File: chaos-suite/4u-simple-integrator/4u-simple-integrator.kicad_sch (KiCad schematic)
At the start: 31 parts

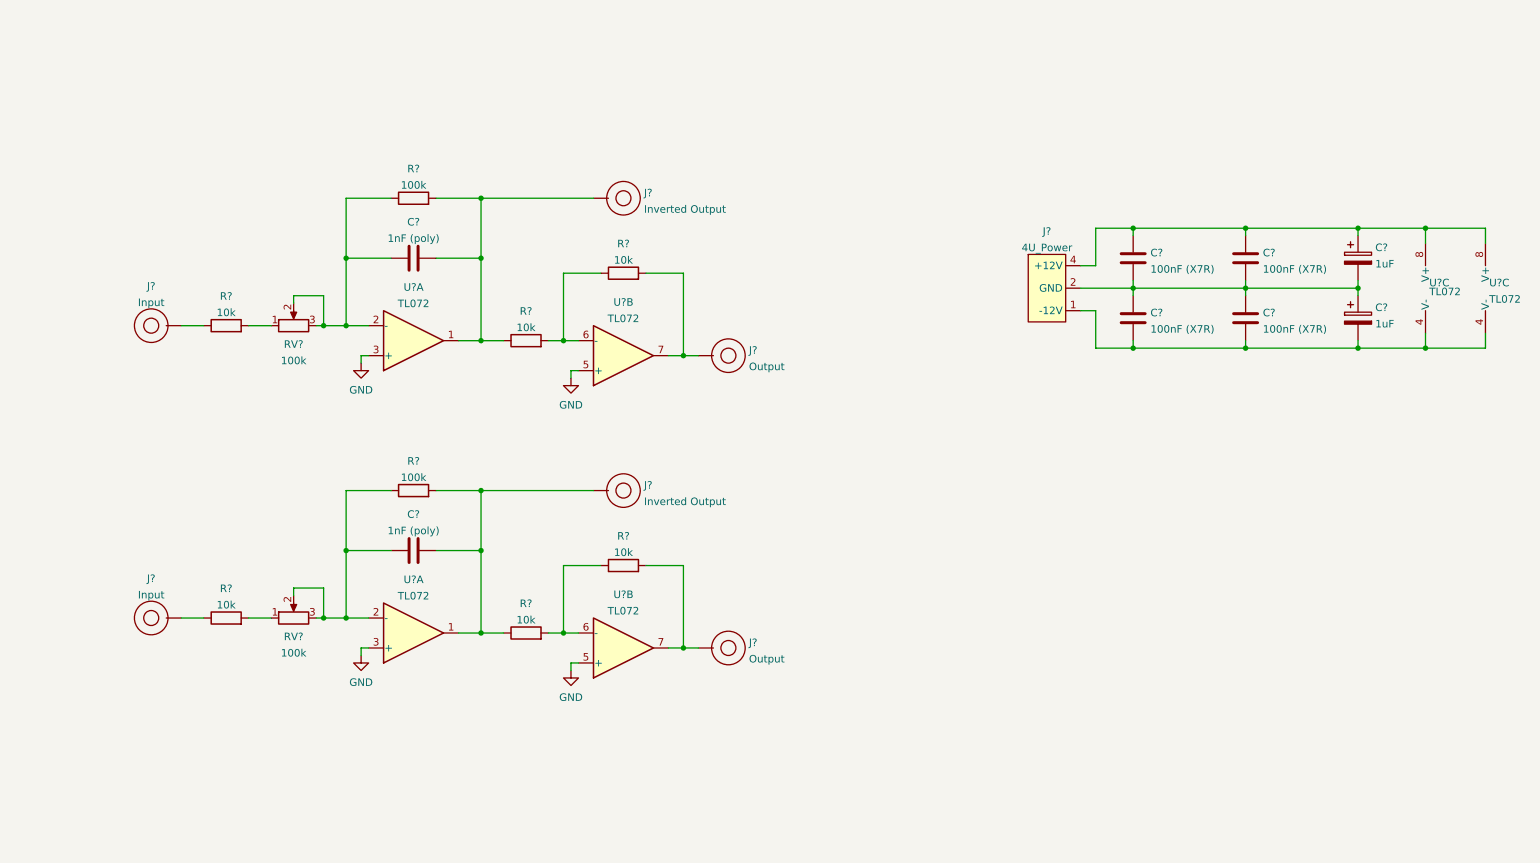
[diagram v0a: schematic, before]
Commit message: Adding first chaos suite modules
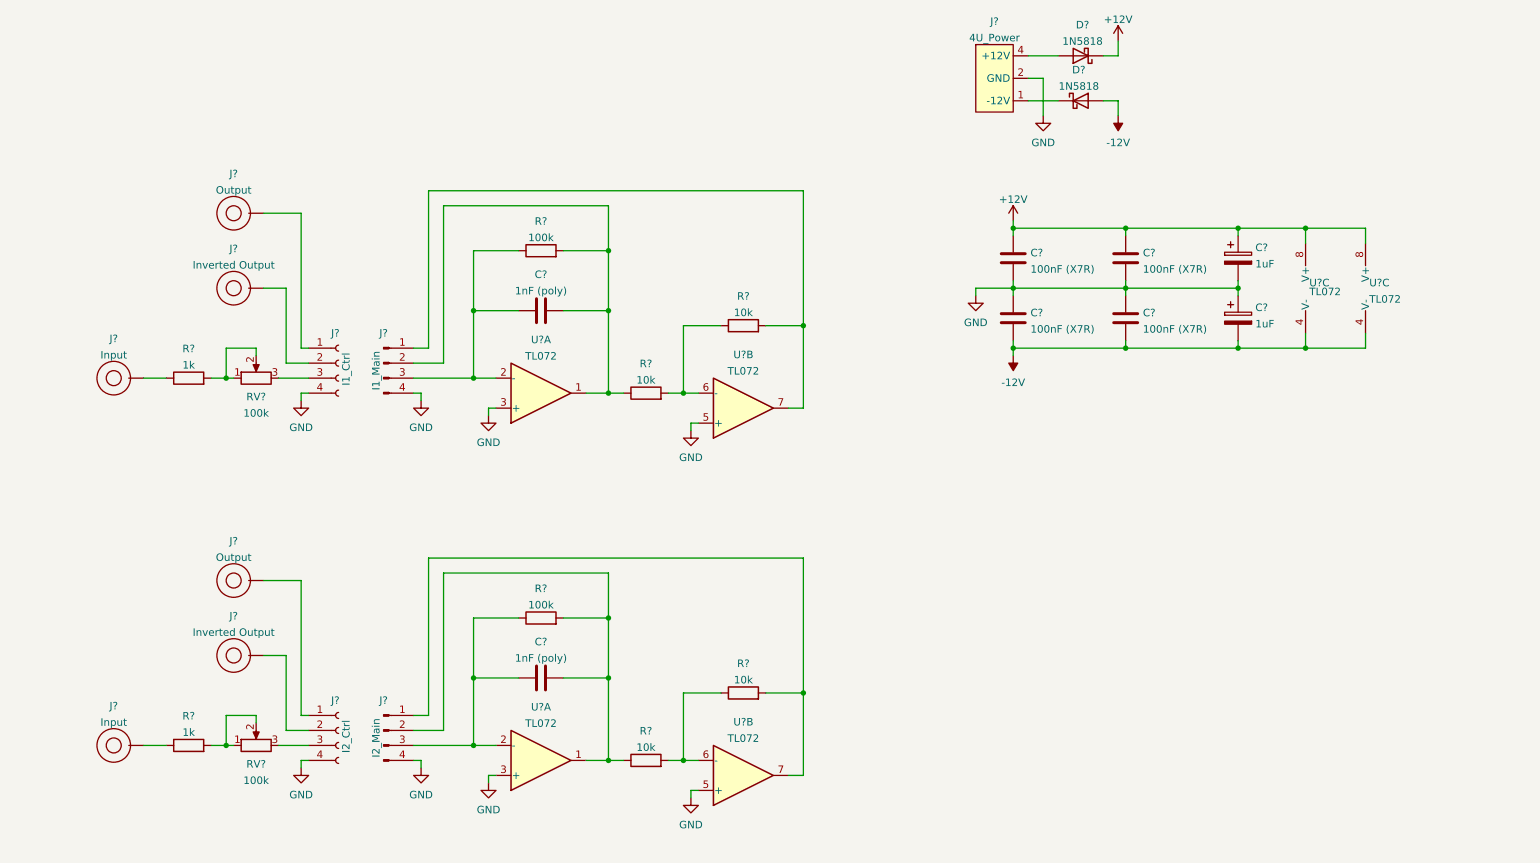
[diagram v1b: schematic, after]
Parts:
- removed C?: 1nF (poly), symbol Device:C
- removed J? (x3): BananaJack_PanelMount, symbol BananaJacks:BananaJack_PanelMount
- removed R?: 100k, symbol Device:R
- removed R? (x3): 10k, symbol Device:R
- removed RV?: 100k, symbol Device:R_Potentiometer
- removed U? (x2): TL072, symbol Amplifier_Operational:TL072
- added C?: 1nF (poly), symbol Device:C
- added D? (x2): 1N5818, Diode_THT:D_DO-41_SOD81_P10.16mm_Horizontal, symbol Diode:1N5818
- added J?: I1_Ctrl, symbol Connector:Conn_01x04_Female
- added J? (x3): BananaJack_PanelMount, symbol BananaJacks:BananaJack_PanelMount
- added J?: I2_Main, symbol Connector:Conn_01x04_Male
- added J?: I2_Ctrl, symbol Connector:Conn_01x04_Female
- added J?: I1_Main, symbol Connector:Conn_01x04_Male
- added R?: 100k, symbol Device:R
- added R? (x2): 10k, symbol Device:R
- added R?: 1k, symbol Device:R
- added RV?: 100k, symbol Device:R_Potentiometer
- added U? (x2): TL072, symbol Amplifier_Operational:TL072
- R?: value 10k -> 1k
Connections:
- net GND: now also C?.1, C?.1, C?.1, C?.2, C?.2, C?.2, J?.2 (GND), J?.3 (GND), J?.4 (Pin_4), J?.4 (Pin_4), J?.4 (Pin_4), J?.4 (Pin_4), U?.3 (+), U?.5 (+)
- net -12V: now reaches C?.2, C?.2, C?.2, U?.4 (V-), U?.4 (V-)
- net -12V: now also D?.2 (A); no longer J?.1 (-12V)
- net +12V: now reaches C?.1, C?.1, C?.1, U?.8 (V+), U?.8 (V+)
- net +12V: now also D?.1 (K); no longer J?.4 (+12V)
- net at C?.2, R?.1, R?.2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: now also J?.2 (Pin_2); no longer J?.1
- net at R?.2, RV?.1: now also RV?.2
- net at C?.1, R?.1, U?.2 (-): now also J?.3 (Pin_3); no longer RV?.2, RV?.3
- net at R?.2, U?.7: now also J?.1 (Pin_1); no longer J?.1
- new net: D?.1 (K), J?.1 (-12V)
- new net: D?.2 (A), J?.4 (+12V)
- new net: J?.1, J?.1 (Pin_1) (x2)
- new net: J?.1, J?.2 (Pin_2) (x2)
- new net: J?.3 (Pin_3), RV?.3 (x2)
- new net: C?.1, J?.3 (Pin_3), R?.1, U?.2 (-)
- new net: C?.2, J?.2 (Pin_2), R?.1, R?.2, U?.1
- new net: R?.1, R?.2, U?.6 (-)
- new net: J?.1 (Pin_1), R?.2, U?.7
- new net: J?.1, R?.1
- new net: R?.2, RV?.1, RV?.2
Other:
- moved on the sheet: C?, J?, R?, RV?, U?A, U?B, U?C

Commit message: Final tweaks to simple integrator
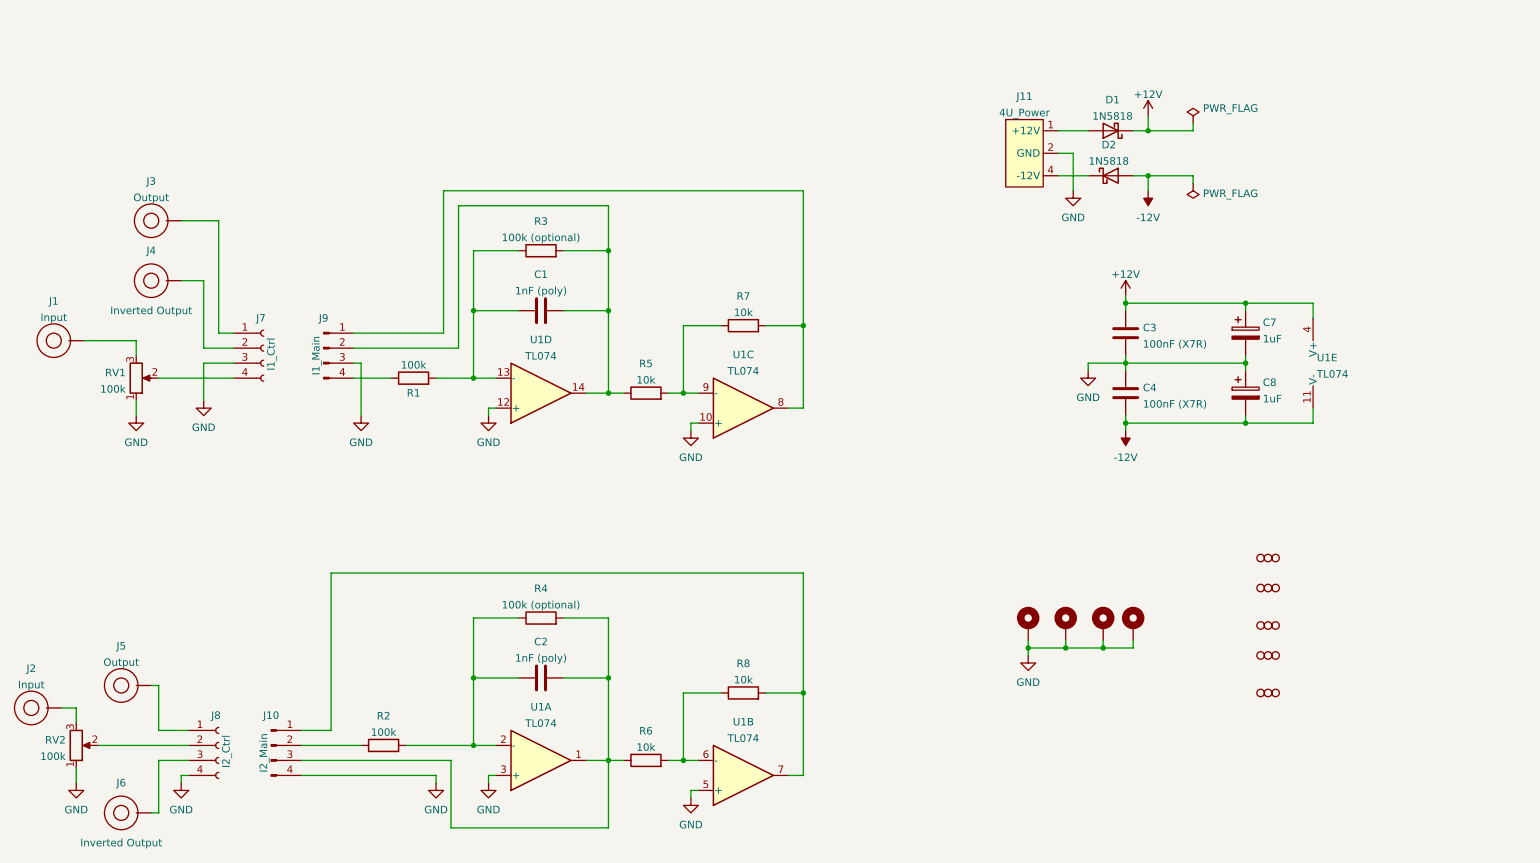
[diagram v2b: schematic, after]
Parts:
- removed C? (x2): 100nF (X7R), symbol Device:C
- removed U? (x6): TL072, symbol Amplifier_Operational:TL072
- added H1, H2, H3, H4: MountingHole_Pad, MountingHole:MountingHole_3.2mm_M3_Pad, symbol Mechanical:MountingHole_Pad
- added H5, H6, H7, H8, H9: MouseBite, Panelization:mouse-bite-2.54mm-slot, symbol Panelization:MouseBite
- added U1: TL074, Rumblesan_Footprints:DIP-14_W7.62mm_Socket, symbol Amplifier_Operational:TL074
- C1, C2, C3, C4: renamed from C?; footprint (none) -> Rumblesan_Footprints:C_Rect_L7.0mm_W3.5mm_P5.00mm
- C7, C8: renamed from C?; footprint (none) -> Capacitor_THT:CP_Radial_D5.0mm_P2.00mm
- D1, D2: renamed from D?; footprint Diode_THT:D_DO-41_SOD81_P10.16mm_Horizontal -> Rumblesan_Footprints:D_DO-41_SOD81_P10.16mm_Horizontal
- J1, J2, J3, J4, J5, J6: renamed from J?; footprint (none) -> Rumblesan_Footprints:BananaJack_THT_JohnsonCinch_108-09
- J10, J9: renamed from J?; footprint (none) -> Connector_PinHeader_2.54mm:PinHeader_1x04_P2.54mm_Vertical
- J11: renamed from J?; footprint (none) -> Rumblesan_Footprints:4u_Power_Molex_KK-254_P2.54mm
- J7, J8: renamed from J?; footprint (none) -> Connector_PinSocket_2.54mm:PinSocket_1x04_P2.54mm_Vertical
- R1, R2: renamed from R?; value 1k -> 100k; footprint (none) -> Rumblesan_Footprints:Resistor_THT_L6.3mm_D2.5mm_P10.16mm_Horizontal
- R3, R4: renamed from R?; value 100k -> 100k (optional); footprint (none) -> Rumblesan_Footprints:Resistor_THT_L6.3mm_D2.5mm_P10.16mm_Horizontal
- R5, R6, R7, R8: renamed from R?; footprint (none) -> Rumblesan_Footprints:Resistor_THT_L6.3mm_D2.5mm_P10.16mm_Horizontal
- RV1, RV2: renamed from RV?; footprint (none) -> Rumblesan_Footprints:Potentiometer_Alpha_RD901F-40-00D_Single_Vertical_CircularHoles
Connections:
- net +12V: now also U1.4 (V+)
- net -12V: now also U1.11 (V-)
- net GND: now also J7.3 (Pin_3), J9.3 (Pin_3), RV1.1, RV2.1, H1.1, H2.1, H3.1, H4.1, U1.10 (+), U1.12 (+), U1.3 (+), U1.5 (+); no longer J7.4 (Pin_4), J9.4 (Pin_4)
- net at J11.1 (+12V): now also D1.2 (A); no longer D2.1 (K)
- net at J11.4 (-12V): now also D2.1 (K); no longer D1.2 (A)
- net at RV1.3: now also J1.1; no longer J7.3 (Pin_3)
- net at J6.1: now also J8.3 (Pin_3); no longer J8.2 (Pin_2)
- net at C2.2, R4.2, R6.1: now also J10.3 (Pin_3), U1.1; no longer J10.2 (Pin_2)
- net at R6.2, R8.1: now also U1.6 (-)
- net at J2.1: now also RV2.3; no longer R2.1
- net at C1.1, R3.1: now also R1.2, U1.13 (-); no longer J9.3 (Pin_3)
- net at C1.2, J9.2 (Pin_2), R3.2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: now also U1.14
- net at J10.1 (Pin_1), R8.2: now also U1.7
- net at C2.1, R4.1: now also R2.2, U1.2 (-); no longer J10.3 (Pin_3)
- net at R5.2, R7.1: now also U1.9 (-)
- net at J9.1 (Pin_1), R7.2: now also U1.8
- net at R1.1: now also J9.4 (Pin_4); no longer J1.1
- new net: J7.4 (Pin_4), RV1.2
- new net: J10.2 (Pin_2), R2.1
- new net: J8.2 (Pin_2), RV2.2
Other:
- title: (none) -> Simple Integrator
- moved on the sheet: C3, C4, C7, C8, D1, D2, J1, J10, J11, J2, J3, J4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

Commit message: Updating simple integrator to rev2
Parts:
- removed H5, H6, H7, H8, H9: MouseBite, Panelization:mouse-bite-2.54mm-slot, symbol Panelization:MouseBite
- added R10, R3, R4, R9: 330r, rumblesan-standard-parts:R_Axial_DIN0207_L6.3mm_D2.5mm_P10.16mm_Horizontal, symbol rumblesan-standard-parts:R
- C1, C2: value 1nF (poly) -> 1nF; footprint Rumblesan_Footprints:C_Rect_L7.0mm_W3.5mm_P5.00mm -> rumblesan-standard-parts:C_Rect_L7.0mm_W3.5mm_P5.00mm; symbol Device:C -> rumblesan-standard-parts:C; Spec (none) -> film; Tolerance (none) -> 5%
- C3, C4: value 100nF (X7R) -> 100nF; footprint Rumblesan_Footprints:C_Rect_L7.0mm_W3.5mm_P5.00mm -> rumblesan-standard-parts:C_Rect_L7.0mm_W3.5mm_P5.00mm; symbol Device:C -> rumblesan-standard-parts:C; Spec (none) -> ceramic X7R; Tolerance (none) -> 5%
- C5: renamed from C7; value 1uF -> 10uF; footprint Capacitor_THT:CP_Radial_D5.0mm_P2.00mm -> rumblesan-standard-parts:CP_Radial_D5.0mm_P2.00mm; symbol Device:C_Polarized -> rumblesan-standard-parts:C_Polarized; Spec (none) -> electrolytic; Tolerance (none) -> 20%; Voltage (none) -> 50v
- C6: renamed from C8; value 1uF -> 10uF; footprint Capacitor_THT:CP_Radial_D5.0mm_P2.00mm -> rumblesan-standard-parts:CP_Radial_D5.0mm_P2.00mm; symbol Device:C_Polarized -> rumblesan-standard-parts:C_Polarized; Spec (none) -> electrolytic; Tolerance (none) -> 20%; Voltage (none) -> 50v
- D1, D2: footprint Rumblesan_Footprints:D_DO-41_SOD81_P10.16mm_Horizontal -> rumblesan-standard-parts:D_DO-41_SOD81_P10.16mm_Horizontal
- H1, H2, H3, H4: now left out of the parts list
- J1: renamed from J2; footprint Rumblesan_Footprints:BananaJack_THT_JohnsonCinch_108-09 -> rumblesan-standard-parts:BananaJack_THT_JohnsonCinch_108-09; symbol BananaJacks:BananaJack_PanelMount -> BananaJacks:Banana Socket PanelMount
- J11: footprint Rumblesan_Footprints:4u_Power_Molex_KK-254_P2.54mm -> 4u-power:4u_Power_Molex_KK-254_P2.54mm
- J2: renamed from J1; footprint Rumblesan_Footprints:BananaJack_THT_JohnsonCinch_108-09 -> rumblesan-standard-parts:BananaJack_THT_JohnsonCinch_108-09; symbol BananaJacks:BananaJack_PanelMount -> BananaJacks:Banana Socket PanelMount
- J3: renamed from J5; footprint Rumblesan_Footprints:BananaJack_THT_JohnsonCinch_108-09 -> rumblesan-standard-parts:BananaJack_THT_JohnsonCinch_108-09; symbol BananaJacks:BananaJack_PanelMount -> BananaJacks:Banana Socket PanelMount
- J4: renamed from J6; footprint Rumblesan_Footprints:BananaJack_THT_JohnsonCinch_108-09 -> rumblesan-standard-parts:BananaJack_THT_JohnsonCinch_108-09; symbol BananaJacks:BananaJack_PanelMount -> BananaJacks:Banana Socket PanelMount
- J5: renamed from J3; footprint Rumblesan_Footprints:BananaJack_THT_JohnsonCinch_108-09 -> rumblesan-standard-parts:BananaJack_THT_JohnsonCinch_108-09; symbol BananaJacks:BananaJack_PanelMount -> BananaJacks:Banana Socket PanelMount
- J6: renamed from J4; footprint Rumblesan_Footprints:BananaJack_THT_JohnsonCinch_108-09 -> rumblesan-standard-parts:BananaJack_THT_JohnsonCinch_108-09; symbol BananaJacks:BananaJack_PanelMount -> BananaJacks:Banana Socket PanelMount
- R1: renamed from R2; footprint Rumblesan_Footprints:Resistor_THT_L6.3mm_D2.5mm_P10.16mm_Horizontal -> rumblesan-standard-parts:R_Axial_DIN0207_L6.3mm_D2.5mm_P10.16mm_Horizontal; symbol Device:R -> rumblesan-standard-parts:R; Power (none) -> 0.5W; Spec (none) -> metal film; Tolerance (none) -> 1%
- R11: renamed from R7; footprint Rumblesan_Footprints:Resistor_THT_L6.3mm_D2.5mm_P10.16mm_Horizontal -> rumblesan-standard-parts:R_Axial_DIN0207_L6.3mm_D2.5mm_P10.16mm_Horizontal; symbol Device:R -> rumblesan-standard-parts:R; Power (none) -> 0.5W; Spec (none) -> metal film; Tolerance (none) -> 1%
- R12: renamed from R8; footprint Rumblesan_Footprints:Resistor_THT_L6.3mm_D2.5mm_P10.16mm_Horizontal -> rumblesan-standard-parts:R_Axial_DIN0207_L6.3mm_D2.5mm_P10.16mm_Horizontal; symbol Device:R -> rumblesan-standard-parts:R; Power (none) -> 0.5W; Spec (none) -> metal film; Tolerance (none) -> 1%
- R2: renamed from R1; footprint Rumblesan_Footprints:Resistor_THT_L6.3mm_D2.5mm_P10.16mm_Horizontal -> rumblesan-standard-parts:R_Axial_DIN0207_L6.3mm_D2.5mm_P10.16mm_Horizontal; symbol Device:R -> rumblesan-standard-parts:R; Power (none) -> 0.5W; Spec (none) -> metal film; Tolerance (none) -> 1%
- R5: renamed from R3; footprint Rumblesan_Footprints:Resistor_THT_L6.3mm_D2.5mm_P10.16mm_Horizontal -> rumblesan-standard-parts:R_Axial_DIN0207_L6.3mm_D2.5mm_P10.16mm_Horizontal; symbol Device:R -> rumblesan-standard-parts:R; Power (none) -> 0.5W; Spec (none) -> metal film; Tolerance (none) -> 1%
- R6: renamed from R4; footprint Rumblesan_Footprints:Resistor_THT_L6.3mm_D2.5mm_P10.16mm_Horizontal -> rumblesan-standard-parts:R_Axial_DIN0207_L6.3mm_D2.5mm_P10.16mm_Horizontal; symbol Device:R -> rumblesan-standard-parts:R; Power (none) -> 0.5W; Spec (none) -> metal film; Tolerance (none) -> 1%
- R7: renamed from R5; footprint Rumblesan_Footprints:Resistor_THT_L6.3mm_D2.5mm_P10.16mm_Horizontal -> rumblesan-standard-parts:R_Axial_DIN0207_L6.3mm_D2.5mm_P10.16mm_Horizontal; symbol Device:R -> rumblesan-standard-parts:R; Power (none) -> 0.5W; Spec (none) -> metal film; Tolerance (none) -> 1%
- R8: renamed from R6; footprint Rumblesan_Footprints:Resistor_THT_L6.3mm_D2.5mm_P10.16mm_Horizontal -> rumblesan-standard-parts:R_Axial_DIN0207_L6.3mm_D2.5mm_P10.16mm_Horizontal; symbol Device:R -> rumblesan-standard-parts:R; Power (none) -> 0.5W; Spec (none) -> metal film; Tolerance (none) -> 1%
- RV1: renamed from RV2; footprint Rumblesan_Footprints:Potentiometer_Alpha_RD901F-40-00D_Single_Vertical_CircularHoles -> rumblesan-standard-parts:Potentiometer_Alpha_RD901F-40-00D_Single_Vertical
- RV2: renamed from RV1; footprint Rumblesan_Footprints:Potentiometer_Alpha_RD901F-40-00D_Single_Vertical_CircularHoles -> rumblesan-standard-parts:Potentiometer_Alpha_RD901F-40-00D_Single_Vertical
- U1: footprint Rumblesan_Footprints:DIP-14_W7.62mm_Socket -> rumblesan-standard-parts:DIP-14_W7.62mm_Socket
- renumbered J9 to J10, J8 to J7, J7 to J8, J10 to J9
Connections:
- net at C1.1, U1.13 (-): now also R2.1, R5.2; no longer R2.2, R5.1
- net at J9.2 (Pin_2): now also R1.2; no longer R1.1
- net at C2.1, U1.2 (-): now also R1.1, R6.2; no longer R1.2, R6.1
- net at J10.4 (Pin_4): now also R2.2; no longer R2.1
- new net: R11.1, R9.1, U1.8
- new net: R11.2, R7.1, U1.9 (-)
- new net: J10.1 (Pin_1), R9.2
- new net: R12.2, R8.1, U1.6 (-)
- new net: C2.2, R3.1, R6.1, R8.2, U1.1
- new net: C1.2, R4.1, R5.1, R7.2, U1.14
- new net: J10.2 (Pin_2), R4.2
- new net: J9.1 (Pin_1), R10.2
- new net: J9.3 (Pin_3), R3.2
- new net: R10.1, R12.1, U1.7
